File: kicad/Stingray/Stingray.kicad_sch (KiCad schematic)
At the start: 47 parts, among them J1 Raspberry_Pi_5, J10 USB_A, J11 Screw_Terminal_01x10, J15 USB_A, J16 USB_A, J17 USB_A, J18 USB_A, J2 Screw_Terminal_01x06, J3 Conn_01x05_Pin, J4 USB_A, J5 Screw_Terminal_01x06, J6 USB_A, J7 USB_A, J8 USB_A, J9 USB_A, K2 Fujitsu_FTR-LYAA005x, M1 Motor_DC, M2 Motor_DC, Q1 IRLZ44N, Q2 IRLZ44N, Q3 IRLZ44N, SW1 RotaryEncoder, SW2 RotaryEncoder, SW3 E-STOP BUTTON

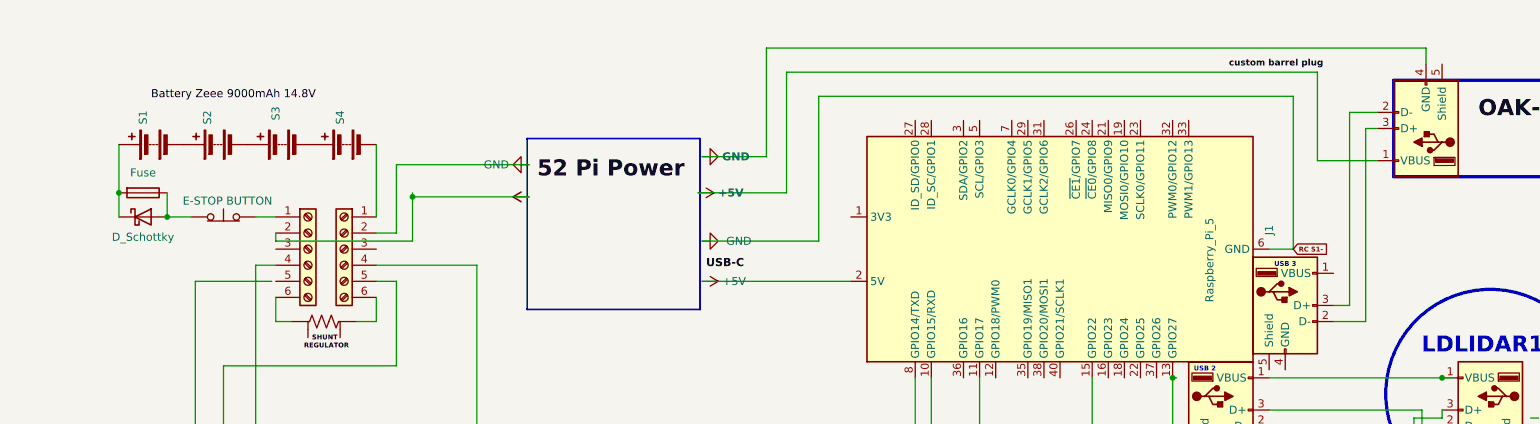
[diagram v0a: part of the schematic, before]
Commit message: docs: FN proofread pt 1 (items 1-~64) + Manual Ch 3.1 STPS source-OR-ing target-topology; kicad Dual Power Input WIP; establish Recap/Remember/Push handoff ritual
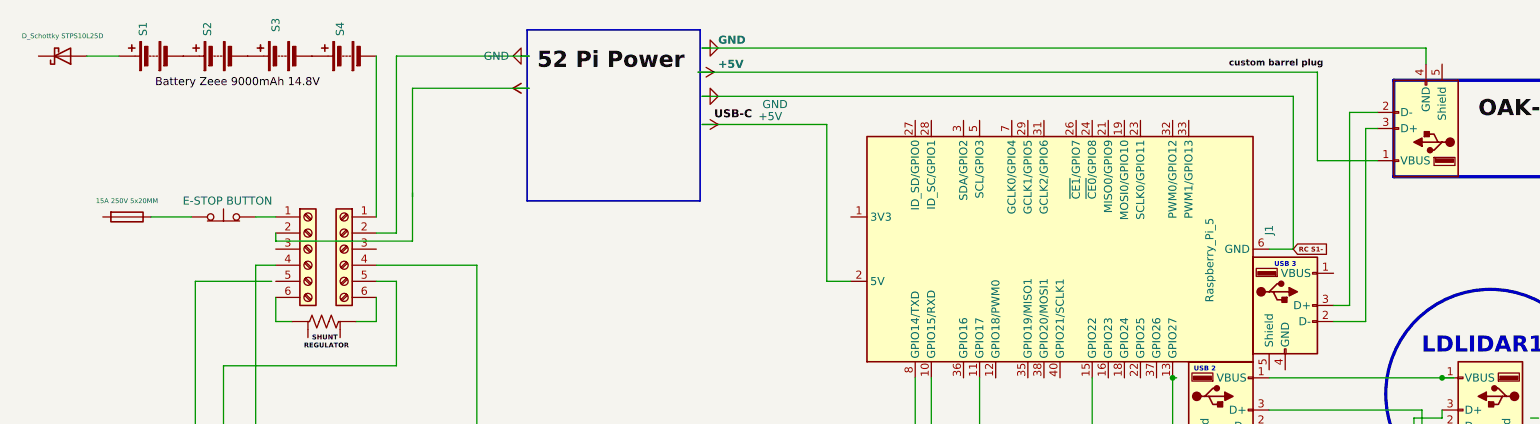
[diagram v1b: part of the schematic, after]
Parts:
- D3: value D_Schottky -> D_Schottky STPS10L25D
- F1: value Fuse -> 15A 250V 5x20MM
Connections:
- net at F1.1, SW3.1 (A): no longer D3.2 (A)
- new net: D3.2 (A), S1.1 (+)
- now unconnected: D3.1 (K), F1.2
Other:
- moved on the sheet: S1, S2, S3, S4

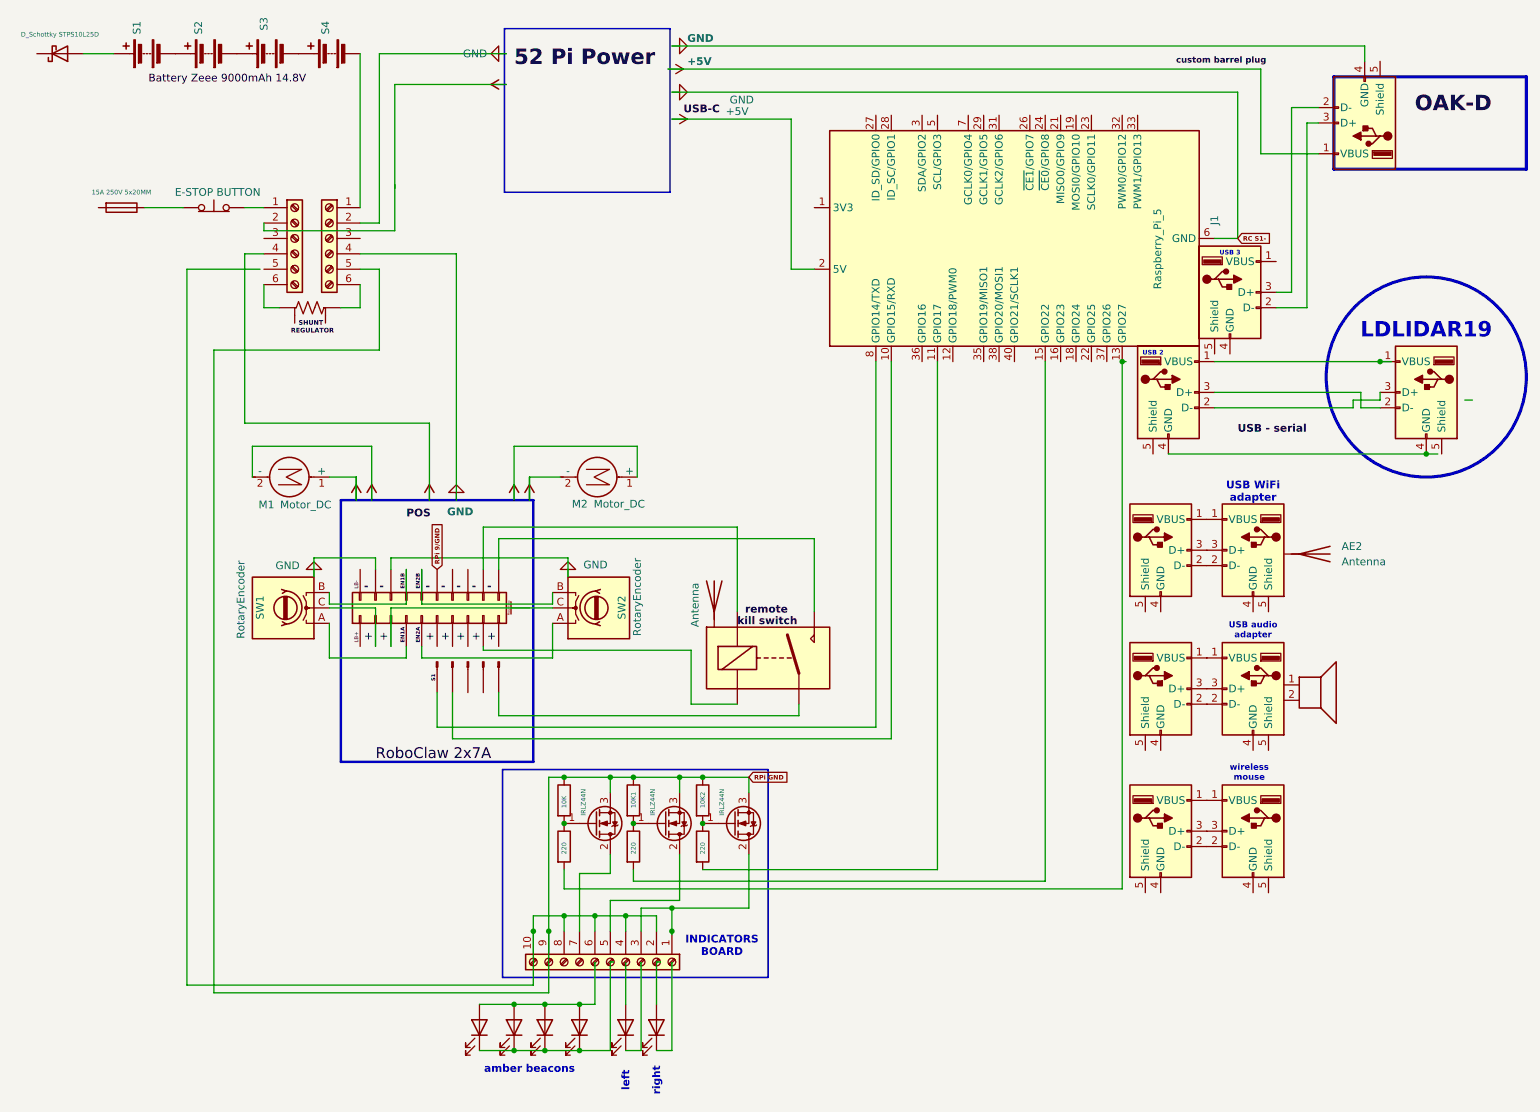
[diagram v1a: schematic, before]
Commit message: v1.2 amend 2026-09-21: right rear Power Input Panel rewire caught up
Manual:
- Ch 2.2 Protection line: 15SQ045 pair (was single STPS10L25D)
- Ch 3.1 Topology: header 'target/in progress' -> 'current, 2026-09-20',
  Status paragraph deleted; topology diode annotation swap to 15SQ045
  with terminal-strip cross-ref
- Ch 3.1 'Fuse-holder proto-board' section rewritten as 'Right rear
  Power Input Panel (2026-09-20, as-built)' - dual PowerPoles, panel
  fuse, 12-pos terminal strip carrying the OR-ing diode pair, RJ45
  keystone jack, bench diode-block field-verification note, four
  assembly photos in stingray build repo, KiCad source refs, and a
  short historical paragraph preserving the pre-rewire proto-board
- Ch 20 BOM Power section: 2 x 15SQ045 + terminal strip + dual
  PowerPole panel-mount + RJ45 keystone (replaces 1 x STPS10L25D)
- Appendix G.9: schematic bumped to 2026.09.20.png; subject updated
  with Dual Power Input panel description; source paths add sub-sheet
- Front-matter version bump 1.1 -> 1.2 with amendment summary

Field Notes:
- FN 22 heading: date list gains 'hardware caught up 2026-09-20'
- FN 22 body: STPS10L25D -> 15SQ045 in the OR-ing description
- FN 22 scope note extended: physical rewire installed 2026-09-20 as
  the right rear Power Input Panel; photos cited
- New FN 22 sub-section 'Part-number footnote': STPS10L25D was pre-
  rewire design intent; 15SQ045 (15 A / 45 V axial) installed for
  higher I/V margin and terminal-strip form factor
- New FN 22 sub-section 'Verifying the OR-ing block with a DMM':
  Sergei's tip explained - reverse-biased Schottky looks like
  ~100 kohm to the DMM's 10 Mohm input; parallel 10 kohm across the
  probes collapses the phantom-voltage reading to a few mV and
  confirms the block. Divider math included.

KiCad source (yesterday's uncommitted work):
- kicad/Stingray/Stingray.kicad_sch, .kicad_pro (top-level sheet)
- kicad/Stingray/Dual Power Input/*.kicad_sch, *.kicad_pro (new
  sub-project for the right re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
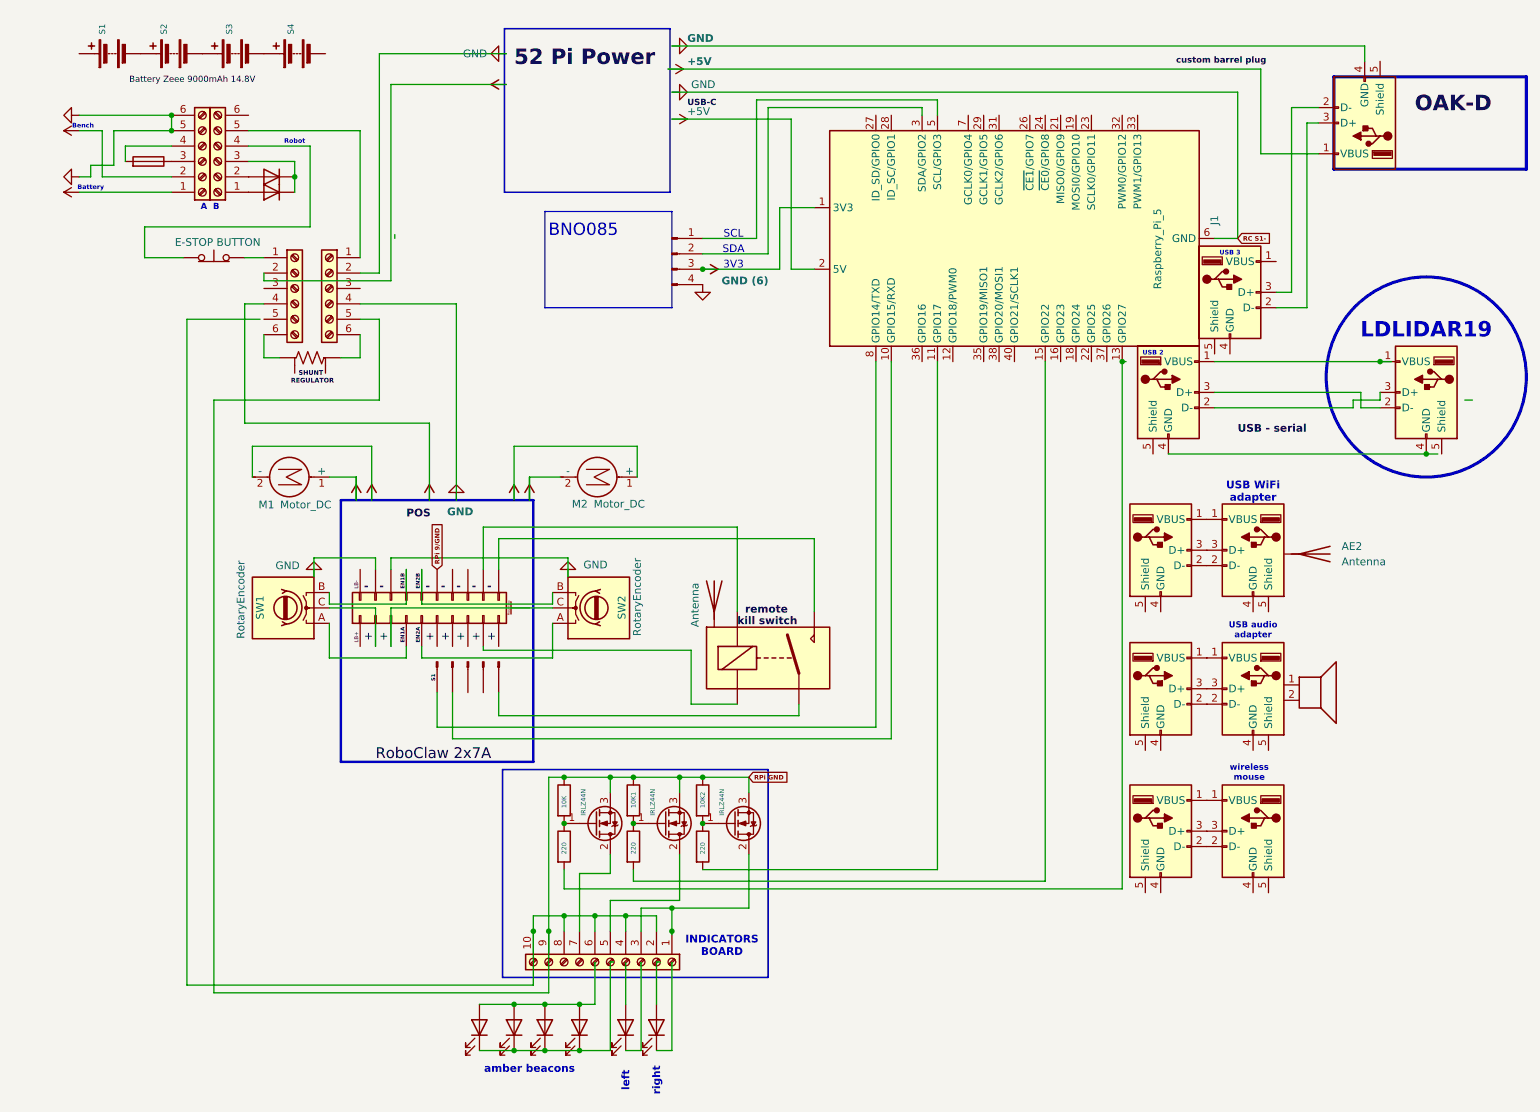
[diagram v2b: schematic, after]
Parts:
- removed D3: D_Schottky STPS10L25D, symbol Device:D_Schottky
- removed F1: 15A 250V 5x20MM, symbol Device:Fuse
- added D8, D9: STPS10L25D, Diode_THT:D_DO-35_SOD27_P7.62mm_Horizontal, symbol Diode:1N914
- added F3: Fuse, symbol Device:Fuse
- added J12, J13: Screw_Terminal_01x06, symbol Connector:Screw_Terminal_01x06
- added J14: Conn_01x04_Pin, symbol Connector:Conn_01x04_Pin
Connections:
- net GND: now also J13.5 (Pin_5), J13.6 (Pin_6)
- net at SW3.1 (A): now also J12.4 (Pin_4)
- net at J5.1 (Pin_1): now also J12.5 (Pin_5); no longer S4.2 (-)
- net at J1.1 (3V3), J1.17 (3V3): now also J14.3 (Pin_3)
- net at J1.3 (SDA/GPIO2): now also J14.2 (Pin_2)
- net at J1.5 (SCL/GPIO3): now also J14.1 (Pin_1)
- new net: D8.1 (K), D9.1 (K), J12.3 (Pin_3)
- new net: D9.2 (A), J12.1 (Pin_1)
- new net: D8.2 (A), J12.2 (Pin_2)
- new net: F3.1, J13.3 (Pin_3)
- new net: F3.2, J13.4 (Pin_4)
- new net +15V: J13.1 (Pin_1), J13.2 (Pin_2)
- new net GND (6): J14.4 (Pin_4)
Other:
- note added: "3V3"
- note added: "A B"
- note added: "BNO085"
- note added: "Battery"
- note added: "Bench"
- note added: "Robot"
- note added: "SCL"
- note added: "SDA"
- moved on the sheet: S1, S2, S3, S4
